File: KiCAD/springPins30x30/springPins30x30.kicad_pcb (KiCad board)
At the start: 2 copper layers, 30 x 30 mm, 21 parts, among them P1 CONN_02X03, P2 CONN_02X03, P3 CONN_02X03, P4 CONN_02X03

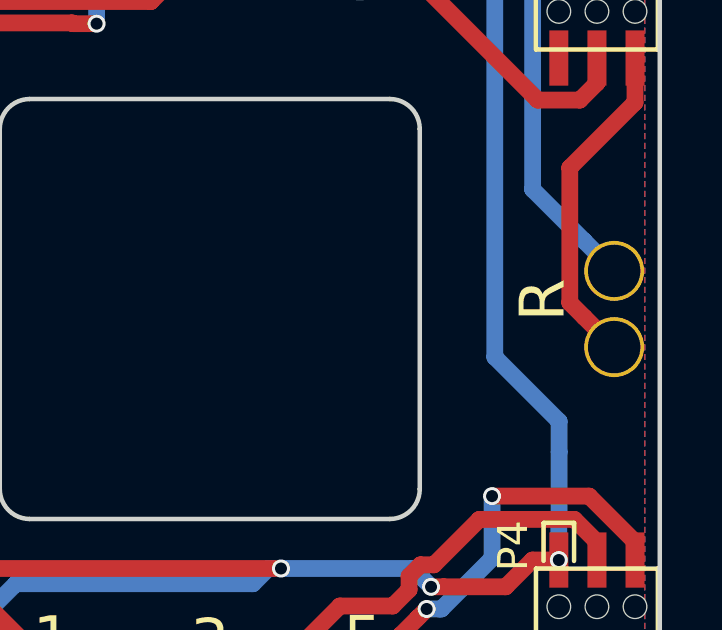
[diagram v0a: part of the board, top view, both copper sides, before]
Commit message: switch to step for 3d
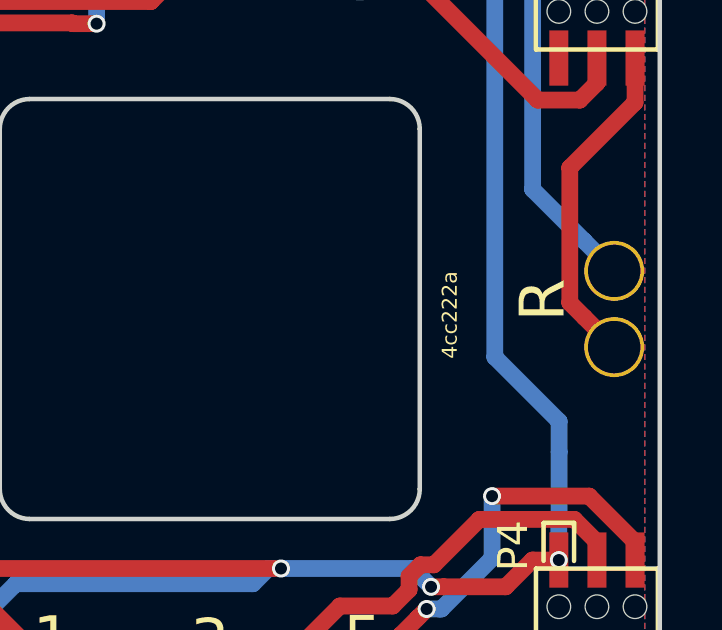
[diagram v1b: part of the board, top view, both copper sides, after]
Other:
- board text added: "4cc222a"

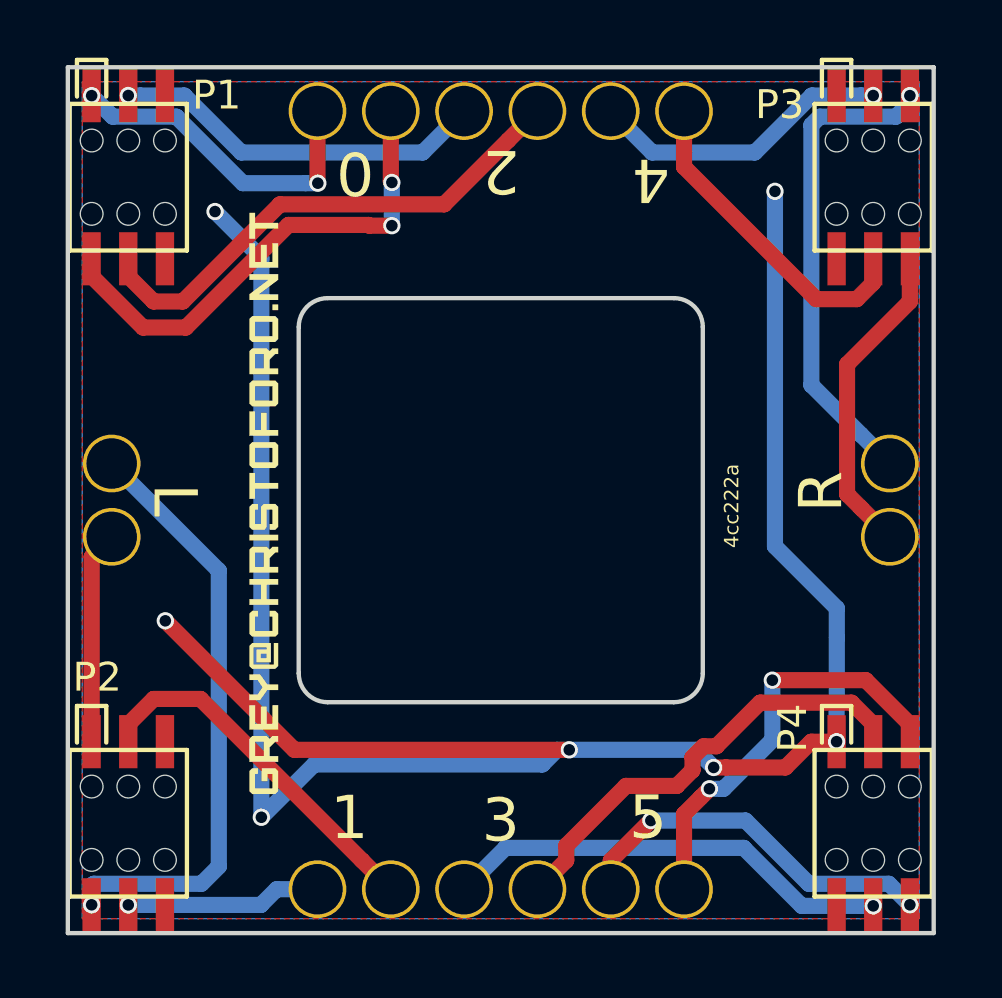
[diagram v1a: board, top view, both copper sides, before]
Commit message: made new photodiode array, fixed springpin board
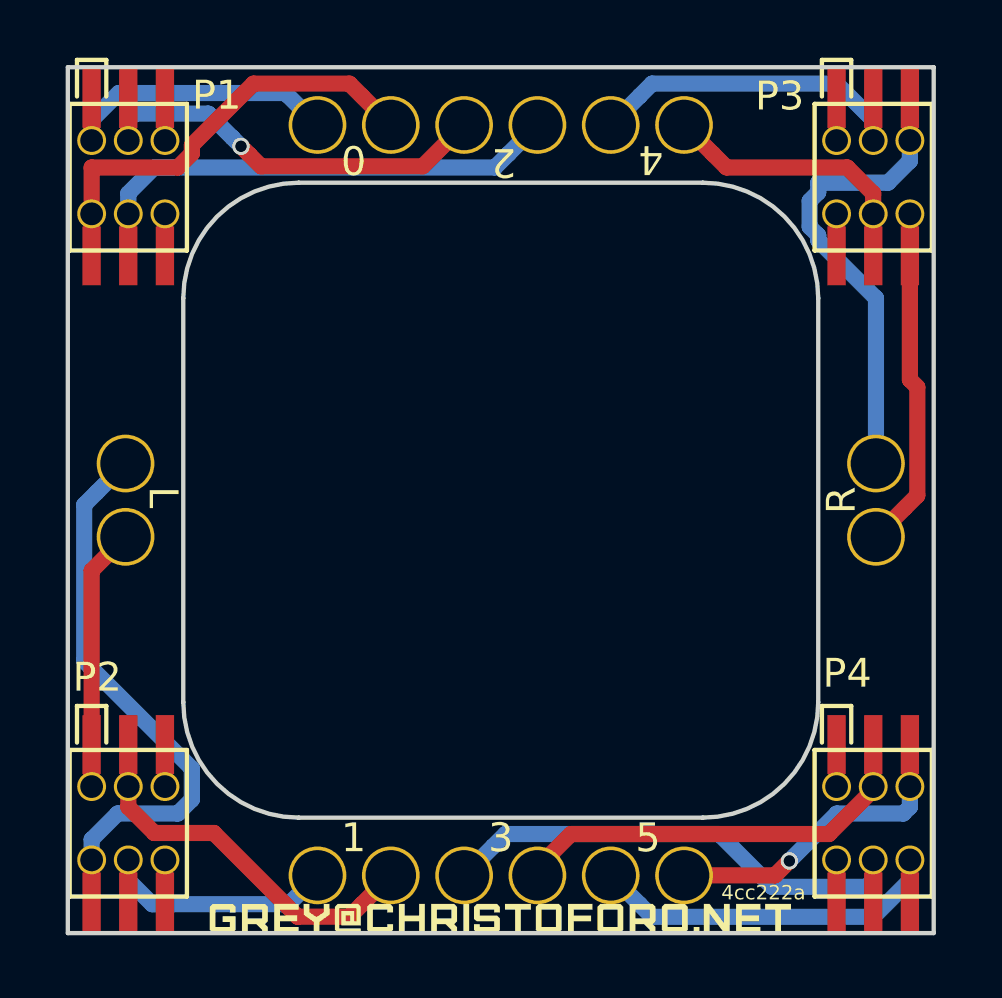
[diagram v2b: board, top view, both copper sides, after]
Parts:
- moved G*** 16.6 mm to (15.0, -0.50), turned to 0 degrees
- moved TP1 0.48 mm to (2.00, -13.7)
- moved TP2 0.48 mm to (2.00, -16.3)
- moved TP11 0.48 mm to (18.8, -28.0)
- moved TP13 0.48 mm to (21.4, -28.0)
- moved TP3 0.48 mm to (8.65, -28.0)
- moved TP5 0.48 mm to (11.2, -28.0)
- moved TP7 0.48 mm to (13.7, -28.0)
- moved TP9 0.48 mm to (16.3, -28.0)
- moved TP10 0.48 mm to (16.3, -2.00)
- moved TP12 0.48 mm to (18.8, -2.00)
- moved TP14 0.48 mm to (21.4, -2.00)
- moved TP4 0.48 mm to (8.65, -2.00)
- moved TP6 0.48 mm to (11.2, -2.00)
- moved TP8 0.48 mm to (13.7, -2.00)
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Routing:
- net GND: track 79.0 -> 1.46 mm, vias 7 -> 0
- net 5_V: track 14.8 -> 11.0 mm, vias 2 -> 1
- net L_V: track 7.39 -> 10.6 mm
- net 1_I: track 6.78 -> 9.48 mm, vias 1 -> 0
- net 2_V: track 13.0 -> 15.2 mm
- net 3_I: track 15.6 -> 17.8 mm, vias 1 -> 0
- net 4_V: track 10.5 -> 12.4 mm, vias 1 -> 0
- net 0_I: track 17.2 -> 15.4 mm, vias 2 -> 0
- net 4_I: track 11.5 -> 9.70 mm
- net /SCK: track 0.00 -> 1.46 mm
- net +5V: track 0.00 -> 1.46 mm
- net +3V3: track 0.00 -> 1.46 mm
- net /SDA: track 0.00 -> 1.46 mm
- net /SCL: track 0.00 -> 1.46 mm
- net /MOSI: track 0.00 -> 1.46 mm
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- removed copper zone on B.Cu, net GND
- removed copper zone on F.Cu, net GND
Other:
- outline, holes or cut-outs redrawn

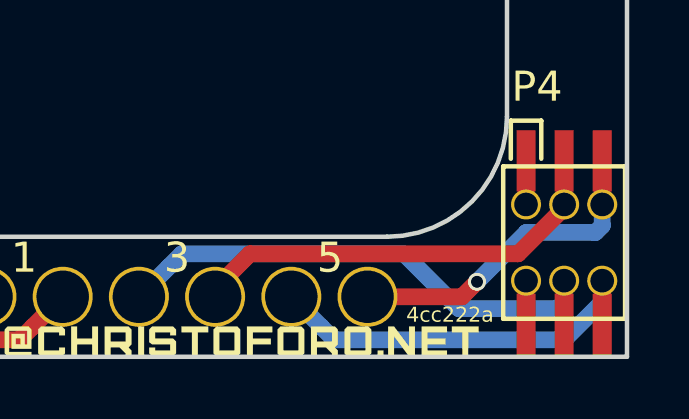
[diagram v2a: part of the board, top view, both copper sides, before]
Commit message: generate order packages
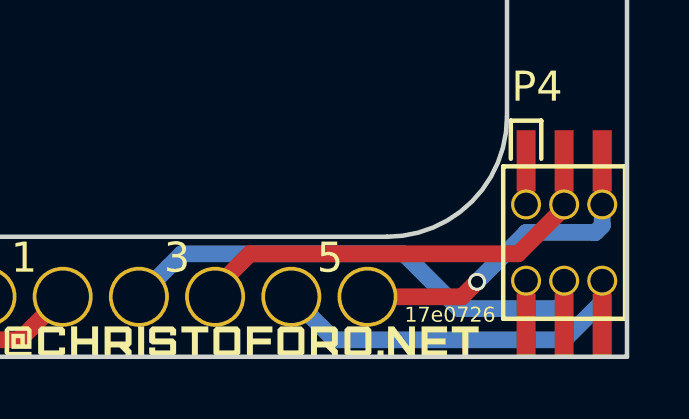
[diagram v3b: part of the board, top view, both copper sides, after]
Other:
- board text added: "17e0726"
- board text removed: "4cc222a"

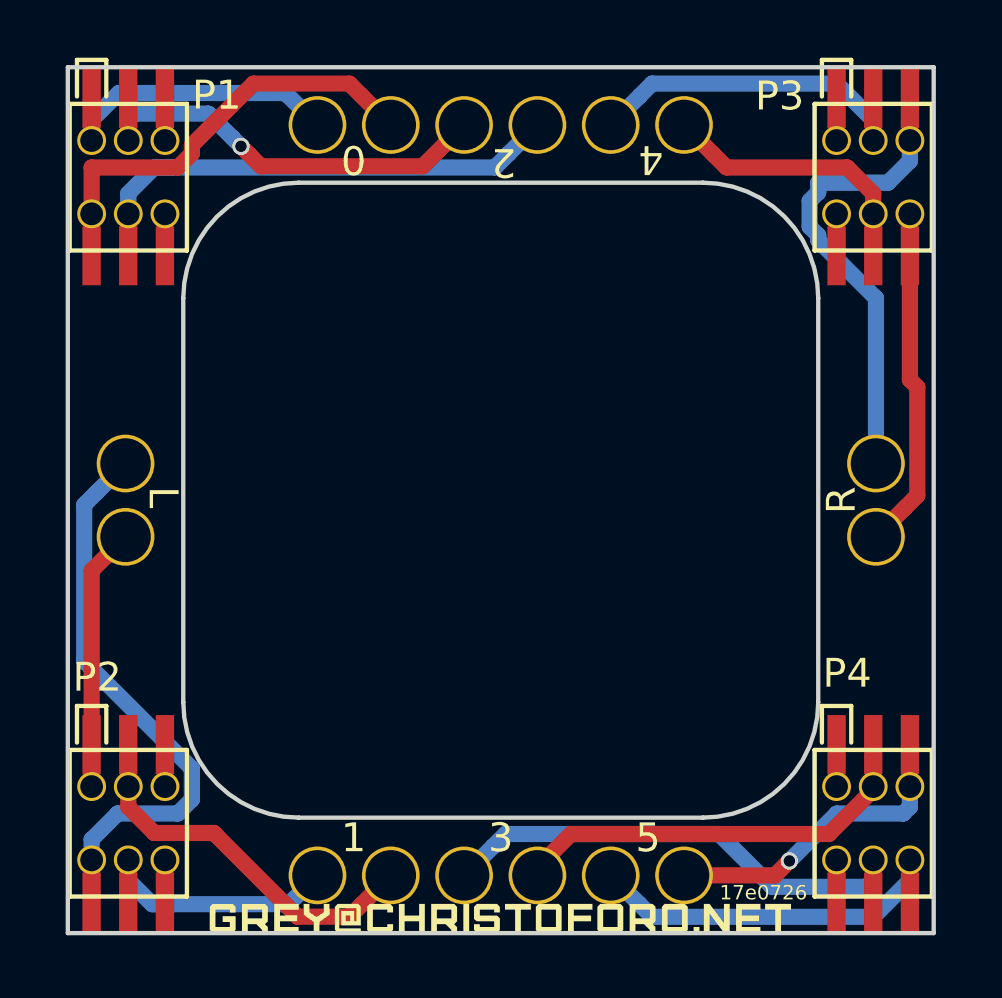
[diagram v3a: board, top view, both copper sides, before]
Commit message: move spring pins out
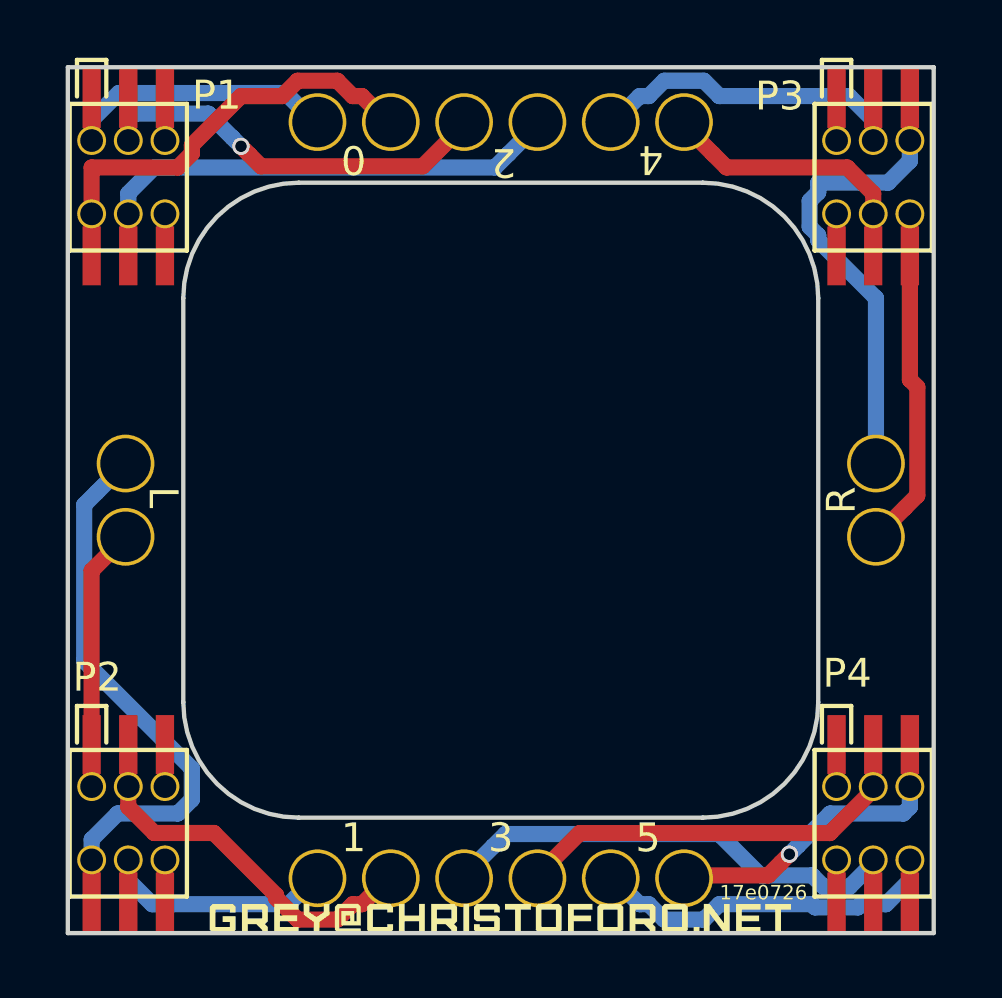
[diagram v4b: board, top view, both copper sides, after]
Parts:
- moved TP11 0.10 mm to (18.8, -28.1)
- moved TP13 0.10 mm to (21.4, -28.1)
- moved TP3 0.10 mm to (8.65, -28.1)
- moved TP5 0.10 mm to (11.2, -28.1)
- moved TP7 0.10 mm to (13.7, -28.1)
- moved TP9 0.10 mm to (16.3, -28.1)
- moved TP10 0.10 mm to (16.3, -1.90)
- moved TP12 0.10 mm to (18.8, -1.90)
- moved TP14 0.10 mm to (21.4, -1.90)
- moved TP4 0.10 mm to (8.65, -1.90)
- moved TP6 0.10 mm to (11.2, -1.90)
- moved TP8 0.10 mm to (13.7, -1.90)

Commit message: update silk
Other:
- board text added: "2004518"
- board text removed: "17e0726"
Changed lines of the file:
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@@
       (xy 4.245503 0.389777) (xy 4.245503 -0.410336)) (layer F.SilkS) (width 0.001))
   )
-  (gr_text 17e0726 (at 24.1 -1.4) (layer F.SilkS)
+  (gr_text 2004518 (at 24.1 -1.4) (layer F.SilkS)
     (effects (font (size 0.5 0.5) (thickness 0.125)))
   )

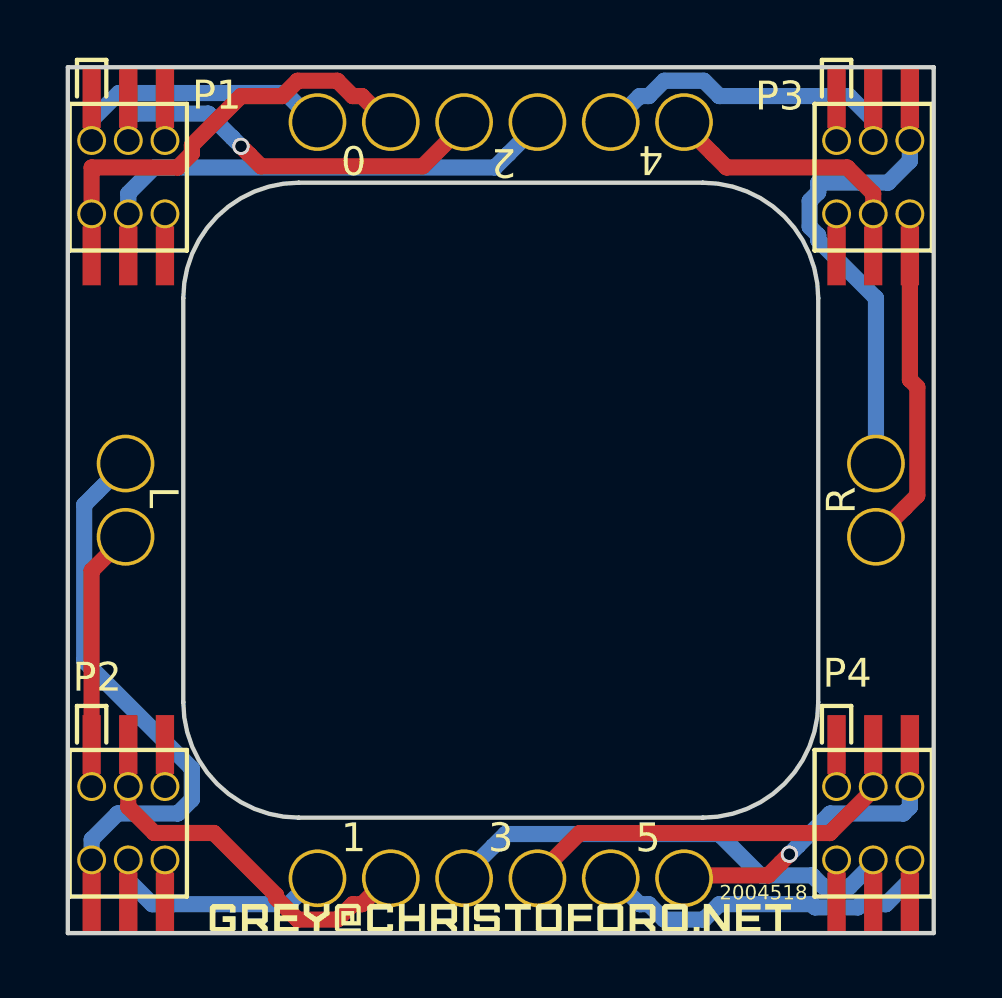
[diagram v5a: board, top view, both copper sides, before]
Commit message: fix pwr/gnd swap, fix extra clock signal name, fix pin hole sizes
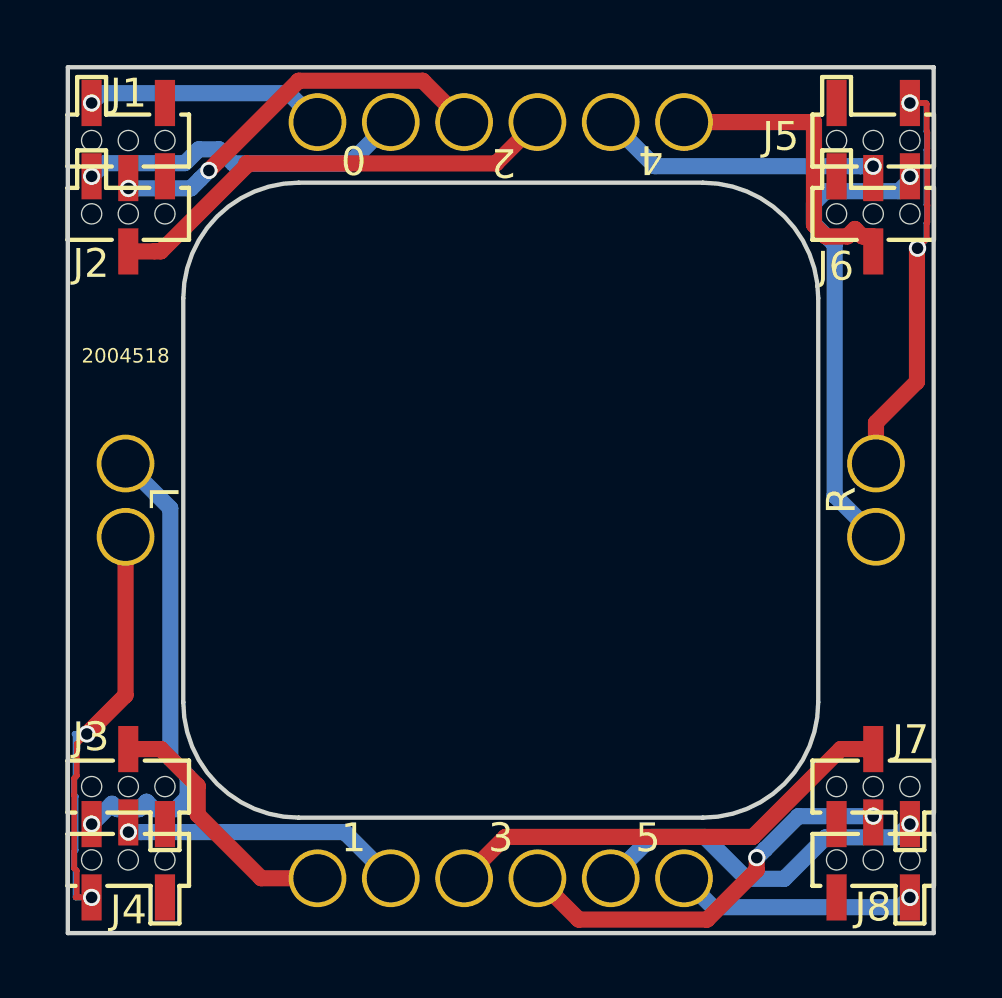
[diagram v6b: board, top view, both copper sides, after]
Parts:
- removed G***: value, myParts:logo_small
- removed P1, P2, P3, P4: CONN_02X03, myParts:RSM-103-02-L-D
- added J1: CONN_01X03, myParts:M50-3130342, F.Cu at (0.82, -27.5)
- added J2: CONN_01X03, myParts:M50-3130342, F.Cu at (0.82, -24.9)
- added J3: CONN_01X03, myParts:M50-3130342, F.Cu at (3.37, -5.08)
- added J4: CONN_01X03, myParts:M50-3130342, F.Cu at (3.37, -2.54)
- added J5: CONN_01X03, myParts:M50-3130342, F.Cu at (26.6, -27.5)
- added J6: CONN_01X03, myParts:M50-3130342, F.Cu at (26.6, -24.9)
- added J7: CONN_01X03, myParts:M50-3130342, F.Cu at (29.2, -5.08)
- added J8: CONN_01X03, myParts:M50-3130342, F.Cu at (29.2, -2.54)
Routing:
- net L_V: track 10.6 -> 20.6 mm, vias 0 -> 2
- net R_I: track 11.9 -> 16.2 mm, vias 0 -> 1
- net 0_I: track 15.5 -> 11.5 mm, vias 0 -> 1
- net 1_V: track 13.6 -> 9.75 mm, vias 0 -> 1
- net L_I: track 20.0 -> 16.5 mm, vias 0 -> 1
- net R_V: track 16.5 -> 19.6 mm, vias 0 -> 2
- net 4_V: track 12.5 -> 9.72 mm, vias 0 -> 1
- net 5_V: track 11.0 -> 8.38 mm
- net 0_V: track 10.8 -> 8.38 mm, vias 0 -> 1
- net 2_V: track 15.2 -> 13.8 mm, vias 1 -> 2
- net 5_I: track 13.8 -> 12.3 mm, vias 0 -> 1
- net GND: track 1.46 -> 0.00 mm
- net /SCK: track 1.46 -> 0.00 mm
- net +5V: track 1.46 -> 0.00 mm
- net +3V3: track 1.46 -> 0.00 mm
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
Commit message: update 30x30 silk
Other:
- board text added: "efbba54"
- board text removed: "2004518"
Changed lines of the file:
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@@
   )
   (setup
-    (last_trace_width 0.2)
+    (last_trace_width 0.25)
     (user_trace_width 0.2)
     (user_trace_width 0.56)
@@
     (effects (font (size 1 1) (thickness 0.25)))
   )
-  (gr_text 2004518 (at 2 -20) (layer F.SilkS)
+  (gr_text efbba54 (at 2 -20) (layer F.SilkS)
     (effects (font (size 0.5 0.5) (thickness 0.125)))
   )
